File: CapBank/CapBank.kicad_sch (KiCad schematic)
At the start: 18 parts

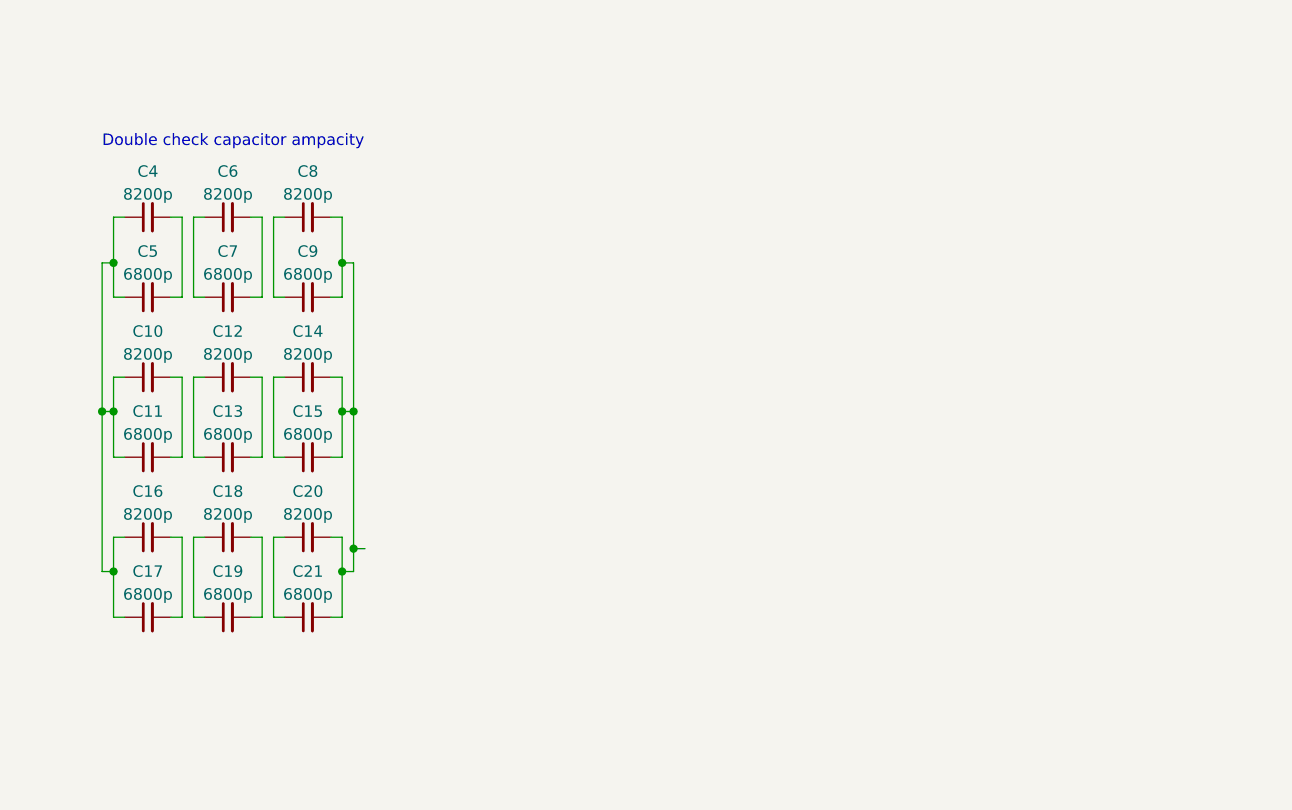
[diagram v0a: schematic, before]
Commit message: Update to improved barrier block and cap bank pcb nearly done
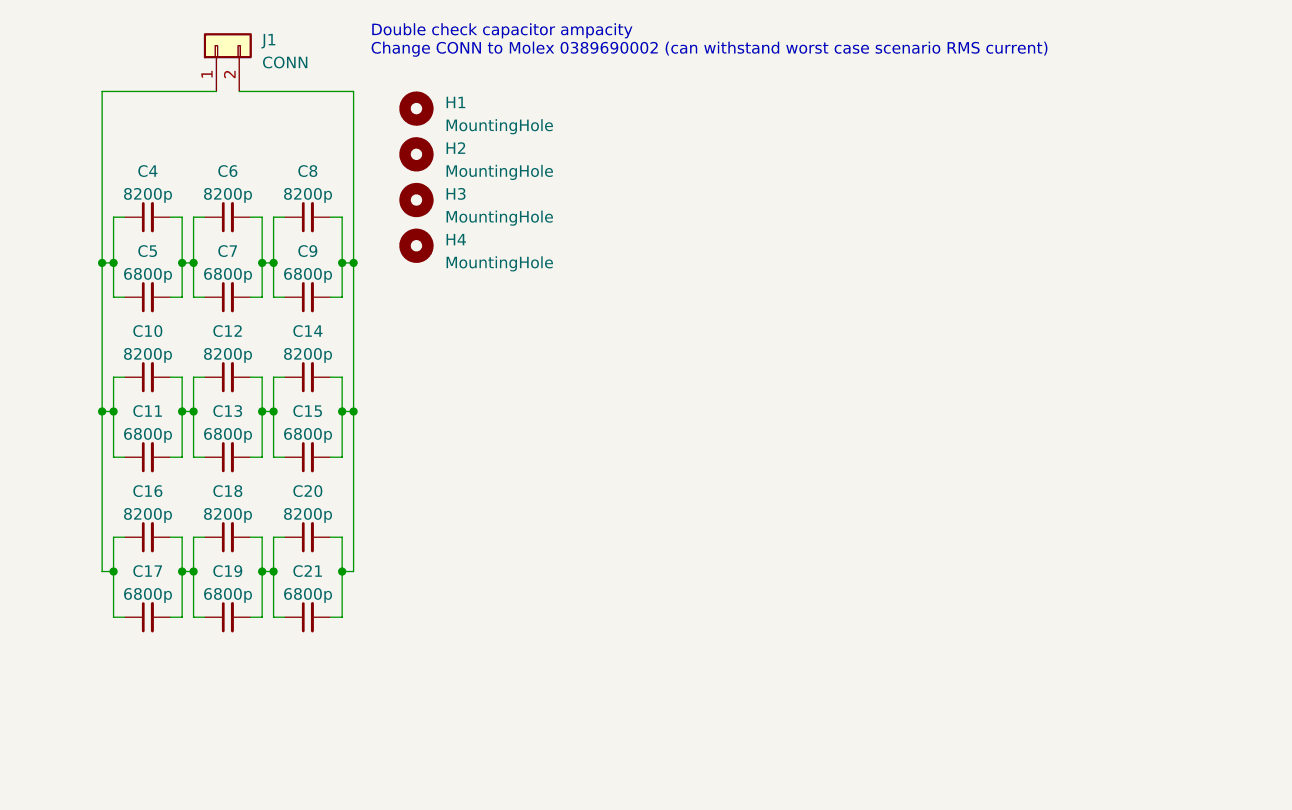
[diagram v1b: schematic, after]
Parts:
- added H1, H2, H3, H4: MountingHole, MountingHole:MountingHole_3.2mm_M3_ISO7380_Pad, symbol Mechanical:MountingHole
- added J1: CONN, BarrierBlock:0389690002, symbol Connector_Generic:Conn_01x02
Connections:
- net at C12.1, C13.1: now also C10.2, C11.2
- net at C12.2, C13.2: now also C14.1, C15.1
- net at C18.1, C19.1: now also C16.2, C17.2
- net at C18.2, C19.2: now also C20.1, C21.1
- net at C10.1, C11.1, C16.1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: now also J1.1 (Pin_1)
- net at C14.2, C15.2, C20.2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: now also J1.2 (Pin_2)
- net at C4.2, C5.2: now also C6.1, C7.1
- net at C8.1, C9.1: now also C6.2, C7.2
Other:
- note added: "Double check capacitor ampacity Change CONN to Molex 0389690002 (can withstand worst case scenario RMS current)"
- note removed: "Double check capacitor ampacity"

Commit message: Changes to cap bank WIP
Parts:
- added C10, C16 (x3), C18, C20, C4: 8200p, Capacitor_SMD:C_2220_5650Metric, symbol Device:C_Small
- added C11, C17 (x3), C19, C21, C5: 6800p, Capacitor_SMD:C_2220_5650Metric, symbol Device:C_Small
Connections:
- net at C14.2, C15.2, C20.2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: now also C20.2, C21.2
- new net: C16.2, C17.2, C18.1, C19.1
- new net: C18.2, C19.2, C20.1, C21.1
- new net: C10.1, C11.1, C16.1, C16.1, C17.1, C17.1, C4.1, C5.1, J1.1 (Pin_1)
- new net: C10.1, C10.2, C11.1, C11.2
- new net: C16.1, C16.2, C17.1, C17.2 (x2)
- new net: C4.1, C4.2, C5.1, C5.2

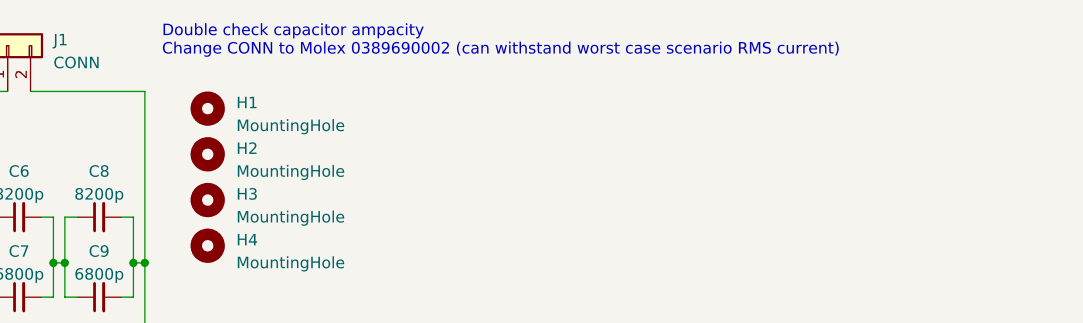
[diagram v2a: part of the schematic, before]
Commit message: Cap bank updated. Vias still WIP
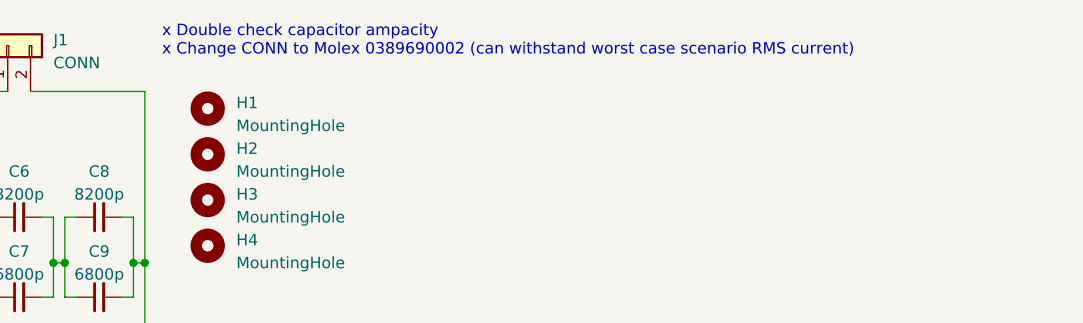
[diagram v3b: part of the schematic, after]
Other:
- note added: "x Double check capacitor ampacity x Change CONN to Molex 0389690002 (can withstand worst case scenario RMS current)"
- note removed: "Double check capacitor ampacity Change CONN to Molex 0389690002 (can withstand worst case scenario RMS current)"
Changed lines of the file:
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@@
     (stroke (width 0) (type default))
   )
-  (text "Double check capacitor ampacity\nChange CONN to Molex 0389690002 (can withstand worst case scenario RMS current)"
+  (text "x Double check capacitor ampacity\nx Change CONN to Molex 0389690002 (can withstand worst case scenario RMS current)"
     (at 141.605 46.355 0)
     (effects (font (size 1.27 1.27)) (justify left bottom))

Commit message: made dimensions multiples of 10 mm
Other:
- note added: "Consider adding fuse to this board"
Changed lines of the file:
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@@
+    (effects (font (size 1.27 1.27)) (justify left bottom))
+  )
+  (text "Consider adding fuse to this board" (at 154.305 81.915 0)
     (effects (font (size 1.27 1.27)) (justify left bottom))
   )
